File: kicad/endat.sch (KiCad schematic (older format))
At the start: 28 parts, among them J1901 tblock2x6, U1901 SI8662BD, U1904 SN75C1168DBR, U1905 SN75C1168DBR, U1908 SI8662BD

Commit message: touting....
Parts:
- added JP1902: jumper, Jumper:SolderJumper-3_P1.3mm_Open_RoundedPad1.0x1.5mm, symbol servo:Jumper_3_Bridged12
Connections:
- net labels added: ENDAT1_CLK_H_N, ENDAT1_CLK_H_P, ENDAT1_DATA_H_N, ENDAT1_DATA_H_P, ENDAT2_CLK_H_N, ENDAT2_CLK_H_P, ENDAT2_DATA_H_N, ENDAT2_DATA_H_P, Earth
- wire segments 180 -> 186
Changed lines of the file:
@@
 	1    0    0    -1
-$EndComp
-Wire Wire Line
-	7900 5450 7900 5400
-$Comp
-L servo:GNDH #PWR?
-U 1 1 5E51CFF4
-P 7900 5450
-AR Path="/5DE49152/5E51CFF4" Ref="#PWR?"  Part="1"
-AR Path="/5E1BAEAA/5E51CFF4" Ref="#PWR?"  Part="1"
-AR Path="/5DE3DF56/5E51CFF4" Ref="#PWR?"  Part="1"
-AR Path="/5F8D42C2/5E51CFF4" Ref="#PWR0222"  Part="1"
-F 0 "#PWR0222" H 7900 5200 30  0001 C CNN
-F 1 "GNDH" H 7900 5292 30  0000 C CNN
-F 2 "" H 7900 5450 50  0001 C CNN
-F 3 "" H 7900 5450 50  0001 C CNN
-	1    7900 5450
-	-1   0    0    -1
 $EndComp
 $Comp
@@
 	8050 4550 8150 4550
 Wire Wire Line
-	7800 5000 8100 5000
-Wire Wire Line
 	7900 5400 8100 5400
 $Comp
@@
 	1    0    0    -1
 $EndComp
-Wire Wire Line
-	7650 5100 8100 5100
-Wire Wire Line
-	7650 5200 7650 5250
-Wire Wire Line
-	7650 5200 8100 5200
-Wire Wire Line
-	7800 5300 8100 5300
-Wire Wire Line
-	8800 5450 8800 5400
-$Comp
-L servo:GNDH #PWR?
-U 1 1 5E607856
-P 8800 5450
-AR Path="/5DE49152/5E607856" Ref="#PWR?"  Part="1"
-AR Path="/5E1BAEAA/5E607856" Ref="#PWR?"  Part="1"
-AR Path="/5DE3DF56/5E607856" Ref="#PWR?"  Part="1"
-AR Path="/5F8D42C2/5E607856" Ref="#PWR0224"  Part="1"
-F 0 "#PWR0224" H 8800 5200 30  0001 C CNN
-F 1 "GNDH" H 8800 5292 30  0000 C CNN
-F 2 "" H 8800 5450 50  0001 C CNN
-F 3 "" H 8800 5450 50  0001 C CNN
-	1    8800 5450
-	1    0    0    -1
-$EndComp
-Wire Wire Line
-	8800 5400 8600 5400
 Text Label 4350 4550 0    39   ~ 0
 ENDAT1_MISO_H
@@
 	7100 4150 7300 4150
 Connection ~ 7300 4150
-Wire Wire Line
-	7650 5050 7650 5100
-Wire Wire Line
-	7800 4950 7800 5000
-Wire Wire Line
-	6850 5050 7200 5050
-Wire Wire Line
-	6750 4950 7100 4950
-Wire Wire Line
-	7100 4150 7100 4950
-Connection ~ 7100 4950
-Wire Wire Line
-	7100 4950 7800 4950
-Connection ~ 7200 5050
-Wire Wire Line
-	7200 5050 7650 5050
 $Comp
 L servo:R_Small R?
@@
 	7450 4150 7650 4150
 Connection ~ 7650 4150
-Wire Wire Line
-	7200 4350 7200 5050
-Wire Wire Line
-	7800 5350 7800 5300
-Wire Wire Line
-	6550 5250 7450 5250
-Wire Wire Line
-	6550 5350 7550 5350
-Wire Wire Line
-	7550 4350 7550 5350
-Connection ~ 7550 5350
-Wire Wire Line
-	7550 5350 7800 5350
-Wire Wire Line
-	7450 4150 7450 5250
-Connection ~ 7450 5250
-Wire Wire Line
-	7450 5250 7650 5250
 NoConn ~ 13850 4250
 NoConn ~ 13850 4650
@@
 NoConn ~ 11250 5250
 NoConn ~ 11250 5350
-Wire Wire Line
-	9050 5100 8600 5100
-Wire Wire Line
-	9050 5200 9050 5250
-Wire Wire Line
-	9050 5200 8600 5200
 $Comp
 L servo:R_Small R?
@@
 	9600 4150 9400 4150
 Connection ~ 9400 4150
-Wire Wire Line
-	9050 5050 9050 5100
-Wire Wire Line
-	9600 4150 9600 4950
-Connection ~ 9600 4950
-Wire Wire Line
-	9600 4950 8900 4950
-Connection ~ 9500 5050
-Wire Wire Line
-	9500 5050 9050 5050
 $Comp
 L servo:R_Small R?
@@
 	9250 4150 9050 4150
 Connection ~ 9050 4150
-Wire Wire Line
-	9500 4350 9500 5050
-Wire Wire Line
-	9150 4350 9150 5350
-Connection ~ 9150 5350
-Wire Wire Line
-	9150 5350 8900 5350
-Wire Wire Line
-	9250 4150 9250 5250
-Connection ~ 9250 5250
-Wire Wire Line
-	9250 5250 9050 5250
-Wire Wire Line
-	8900 4950 8900 5000
-Wire Wire Line
-	8900 5000 8600 5000
-Wire Wire Line
-	8600 5300 8900 5300
-Wire Wire Line
-	8900 5300 8900 5350
-Wire Wire Line
-	9500 5050 9900 5050
-Wire Wire Line
-	9600 4950 10000 4950
-Wire Wire Line
-	9250 5250 10200 5250
-Wire Wire Line
-	9150 5350 10200 5350
+$Comp
+L servo:GNDH #PWR?
+U 1 1 5E31EAC9
+P 8700 5800
+AR Path="/5DDE8C5E/5E31EAC9" Ref="#PWR?"  Part="1"
+AR Path="/5E092156/5E31EAC9" Ref="#PWR?"  Part="1"
+AR Path="/5F8D42C2/5E31EAC9" Ref="#PWR0268"  Part="1"
+F 0 "#PWR0268" H 8700 5550 30  0001 C CNN
+F 1 "GNDH" H 8700 5650 20  0000 C CNN
+F 2 "" H 8700 5800 50  0001 C CNN
+F 3 "" H 8700 5800 50  0001 C CNN
+	1    8700 5800
+	-1   0    0    -1
+$EndComp
+$Comp
+L servo:Jumper_3_Bridged12 JP?
+U 1 1 5E31EACF
+P 8350 5700
+AR Path="/5E1BAEAA/5E31EACF" Ref="JP?"  Part="1"
+AR Path="/5E21534F/5E31EACF" Ref="JP?"  Part="1"
+AR Path="/5DE3DF56/5E31EACF" Ref="JP?"  Part="1"
+AR Path="/5F8D42C2/5E31EACF" Ref="JP1902"  Part="1"
+F 0 "JP1902" H 8350 5869 39  0000 C CNN
+F 1 "jumper" H 8350 5794 39  0000 C CNN
+F 2 "Jumper:SolderJumper-3_P1.3mm_Open_RoundedPad1.0x1.5mm" H 8150 5500 50  0001 C CNN
+F 3 "~" H 8250 5600 50  0001 C CNN
+	1    8350 5700
+	1    0    0    1
+$EndComp
+Wire Wire Line
+	8550 5700 8700 5700
+Wire Wire Line
+	8700 5700 8700 5800
+$Comp
+L servo:Earth #PWR?
+U 1 1 5E31EAD8
+P 8000 5800
+AR Path="/5E21534F/5E31EAD8" Ref="#PWR?"  Part="1"
+AR Path="/5DE3DF56/5E31EAD8" Ref="#PWR?"  Part="1"
+AR Path="/5F8D42C2/5E31EAD8" Ref="#PWR0269"  Part="1"
+F 0 "#PWR0269" H 8000 5550 20  0001 C CNN
+F 1 "Earth" H 8000 5650 20  0000 C CNN
+F 2 "" H 8000 5800 50  0001 C CNN
+F 3 "~" H 8000 5800 50  0001 C CNN
+	1    8000 5800
+	1    0    0    -1
+$EndComp
+Wire Wire Line
+	8150 5700 8000 5700
+Wire Wire Line
+	8000 5700 8000 5850
+Wire Wire Line
+	7900 5600 8350 5600
+Wire Wire Line
+	7900 5400 7900 5600
+Wire Wire Line
+	8800 5400 8800 5600
+Connection ~ 8350 5600
+Wire Wire Line
+	8350 5600 8800 5600
+Text Label 6900 4950 0    39   ~ 0
+ENDAT1_DATA_H_P
+Text Label 6900 5050 0    39   ~ 0
+ENDAT1_DATA_H_N
+Text Label 6850 5350 0    39   ~ 0
+ENDAT1_CLK_H_P
+Text Label 6850 5250 0    39   ~ 0
+ENDAT1_CLK_H_N
+Wire Wire Line
+	6750 4950 7450 4950
+Wire Wire Line
+	7450 4150 7450 4950
+Wire Wire Line
+	7550 4350 7550 5050
+Wire Wire Line
+	6850 5050 7550 5050
+Connection ~ 7550 5050
+Wire Wire Line
+	7550 5050 7800 5050
+Wire Wire Line
+	6550 5250 7200 5250
+Wire Wire Line
+	6550 5350 7100 5350
+Wire Wire Line
+	7100 4150 7100 5350
+Wire Wire Line
+	7200 4350 7200 5250
+Wire Wire Line
+	7100 5350 7950 5350
+Wire Wire Line
+	7950 5350 7950 5000
+Wire Wire Line
+	7950 5000 8100 5000
+Connection ~ 7100 5350
+Wire Wire Line
+	7200 5250 8000 5250
+Wire Wire Line
+	8000 5250 8000 5100
+Wire Wire Line
+	8000 5100 8100 5100
+Connection ~ 7200 5250
+Wire Wire Line
+	7450 4950 7900 4950
+Wire Wire Line
+	7900 4950 7900 5200
+Wire Wire Line
+	7900 5200 8100 5200
+Connection ~ 7450 4950
+Wire Wire Line
+	7800 5050 7800 5300
+Wire Wire Line
+	7800 5300 8100 5300
+Wire Wire Line
+	8600 5000 8900 5000
+Wire Wire Line
+	8900 5000 8900 5350
+Wire Wire Line
+	8850 5250 8850 5100
+Wire Wire Line
+	8850 5100 8600 5100
+Wire Wire Line
+	9000 4950 9000 5200
+Wire Wire Line
+	9000 5200 8600 5200
+Wire Wire Line
+	8600 5300 9050 5300
+Wire Wire Line
+	9050 5300 9050 5050
+Wire Wire Line
+	8850 5250 9500 5250
+Wire Wire Line
+	9150 4350 9150 5050
+Wire Wire Line
+	9050 5050 9150 5050
+Connection ~ 9150 5050
+Wire Wire Line
+	9150 5050 9900 5050
+Wire Wire Line
+	9250 4150 9250 4950
+Wire Wire Line
+	9000 4950 9250 4950
+Connection ~ 9250 4950
+Wire Wire Line
+	9250 4950 10000 4950
+Wire Wire Line
+	9500 4350 9500 5250
+Connection ~ 9500 5250
+Wire Wire Line
+	9500 5250 10200 5250
+Wire Wire Line
+	9600 4150 9600 5350
+Wire Wire Line
+	8900 5350 9600 5350
+Connection ~ 9600 5350
+Wire Wire Line
+	9600 5350 10200 5350
+Text Label 9350 4950 0    39   ~ 0
+ENDAT2_DATA_H_P
+Text Label 9350 5050 0    39   ~ 0
+ENDAT2_DATA_H_N
+Text Label 9250 5250 0    39   ~ 0
+ENDAT2_CLK_H_N
+Text Label 9250 5350 0    39   ~ 0
+ENDAT2_CLK_H_P
+Wire Wire Line
+	8600 5400 8800 5400
 $EndSCHEMATC

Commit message: roouting and more routing.... I think 4 layers WONT be enought
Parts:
- removed JP1901: jumper, Jumper:SolderJumper-3_P1.3mm_Open_RoundedPad1.0x1.5mm, symbol servo:Jumper_3_Bridged12
- added JP1901: jumper, servo:SolderJumper-2_P1.3mm_Open_RoundedPad1.0x1.5mm, symbol servo:jumper
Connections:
- net labels added: ENDAT_5VH
- net labels removed: 15VH
- wire segments 186 -> 185
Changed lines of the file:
@@
 	1    0    0    -1
 $EndComp
-$Comp
-L servo:Jumper_3_Bridged12 JP?
-U 1 1 5E51CFFA
-P 8350 4550
-AR Path="/5E1BAEAA/5E51CFFA" Ref="JP?"  Part="1"
-AR Path="/5DE3DF56/5E51CFFA" Ref="JP?"  Part="1"
-AR Path="/5F8D42C2/5E51CFFA" Ref="JP1901"  Part="1"
-F 0 "JP1901" H 8350 4719 39  0000 C CNN
-F 1 "jumper" H 8350 4644 39  0000 C CNN
-F 2 "Jumper:SolderJumper-3_P1.3mm_Open_RoundedPad1.0x1.5mm" H 8150 4350 50  0001 C CNN
-F 3 "~" H 8250 4450 50  0001 C CNN
-	1    8350 4550
-	1    0    0    -1
-$EndComp
-$Comp
-L servo:15VH #PWR?
-U 1 1 5E51D001
-P 8650 4500
-AR Path="/5E1BAEAA/5E51D001" Ref="#PWR?"  Part="1"
-AR Path="/5DE3DF56/5E51D001" Ref="#PWR?"  Part="1"
-AR Path="/5F8D42C2/5E51D001" Ref="#PWR0223"  Part="1"
-F 0 "#PWR0223" H 8650 4300 20  0001 C CNN
-F 1 "15VH" H 8650 4657 28  0000 C CNN
-F 2 "" H 8650 4500 50  0001 C CNN
-F 3 "" H 8650 4500 50  0001 C CNN
-	1    8650 4500
-	1    0    0    -1
-$EndComp
-Wire Wire Line
-	8650 4550 8650 4500
-Wire Wire Line
-	8550 4550 8650 4550
 Wire Wire Line
 	8050 4500 8050 4550
@@
 	7950 4900 7950 4650
 Wire Wire Line
-	7950 4650 8350 4650
-Wire Wire Line
-	8350 4650 8750 4650
-Wire Wire Line
 	8750 4650 8750 4900
 Wire Wire Line
 	8750 4900 8600 4900
-Connection ~ 8350 4650
 Wire Wire Line
 	4300 4150 7000 4150
@@
 L servo:Earth #PWR?
 U 1 1 5E31EAD8
-P 8000 5800
+P 8050 5800
 AR Path="/5E21534F/5E31EAD8" Ref="#PWR?"  Part="1"
 AR Path="/5DE3DF56/5E31EAD8" Ref="#PWR?"  Part="1"
 AR Path="/5F8D42C2/5E31EAD8" Ref="#PWR0269"  Part="1"
-F 0 "#PWR0269" H 8000 5550 20  0001 C CNN
-F 1 "Earth" H 8000 5650 20  0000 C CNN
-F 2 "" H 8000 5800 50  0001 C CNN
-F 3 "~" H 8000 5800 50  0001 C CNN
-	1    8000 5800
-	1    0    0    -1
-$EndComp
-Wire Wire Line
-	8150 5700 8000 5700
-Wire Wire Line
-	8000 5700 8000 5850
+F 0 "#PWR0269" H 8050 5550 20  0001 C CNN
+F 1 "Earth" H 8050 5650 20  0000 C CNN
+F 2 "" H 8050 5800 50  0001 C CNN
+F 3 "~" H 8050 5800 50  0001 C CNN
+	1    8050 5800
+	1    0    0    -1
+$EndComp
 Wire Wire Line
 	7900 5600 8350 5600
@@
 Wire Wire Line
 	8600 5400 8800 5400
+$Comp
+L servo:jumper JP?
+U 1 1 5E2E6204
+P 8250 4550
+AR Path="/5DD76B18/5E2E6204" Ref="JP?"  Part="1"
+AR Path="/5F8D42C2/5E2E6204" Ref="JP1901"  Part="1"
+F 0 "JP1901" H 8250 4711 39  0000 C CNN
+F 1 "jumper" H 8250 4636 39  0000 C CNN
+F 2 "servo:SolderJumper-2_P1.3mm_Open_RoundedPad1.0x1.5mm" H 8150 4530 50  0001 C CNN
+F 3 "~" H 8250 4630 50  0001 C CNN
+	1    8250 4550
+	1    0    0    -1
+$EndComp
+Wire Wire Line
+	7950 4650 8350 4650
+Wire Wire Line
+	8350 4550 8350 4650
+Connection ~ 8350 4650
+Wire Wire Line
+	8350 4650 8750 4650
+Wire Wire Line
+	8050 5800 8050 5700
+Wire Wire Line
+	8050 5700 8150 5700
+Text Label 8450 4650 0    20   ~ 0
+ENDAT_5VH
 $EndSCHEMATC

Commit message: ROUTING DONE!!!!!!!!!!!!!!!!!!!!!!!!!
ok, but....I need to improve all the nets, get them wider and so, but at
least all nets were routed to the uController.. it was more difucult
than I ever imagine... it tooks me 1 week only the uC coarse layout..
very very complex.. a lot of traces.. and with NO blind vias.. so it'll
be cheaper and any prototype manufacturer could do the board, and it'll
be more reliable..AND I'd test all nets on the board it it has at least
one via, or rout alongside top or bottom, so it's all the nets.. for
debug, it's very important...
lets do some improvement...
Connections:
- net ENDAT1_MOSI_H: no longer U1901.15 (B1), U1904.15 (1D)
- new net: U1901.15 (B1), U1904.15 (1D)
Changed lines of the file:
@@
 Text Label 4350 4550 0    39   ~ 0
 ENDAT1_MISO_H
-Text Label 4350 4150 0    39   ~ 0
+Text Label 3200 4000 0    39   ~ 0
 ENDAT1_MOSI_H
 Text Label 4350 4450 0    39   ~ 0

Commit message: improvement...
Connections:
- net ENDAT1_MOSI_H: now also U1901.15 (B1), U1904.15 (1D)
- net ENDAT_GND: now reaches J1901.6a (Pin_6a), J1901.6b (Pin_6b), JP1902.2 (C)
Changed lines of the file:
@@
 Text Label 8450 4650 0    20   ~ 0
 ENDAT_5VH
+Text Label 8400 5600 0    20   ~ 0
+ENDAT_GND
+Text Label 4350 4150 0    39   ~ 0
+ENDAT1_MOSI_H
 $EndSCHEMATC

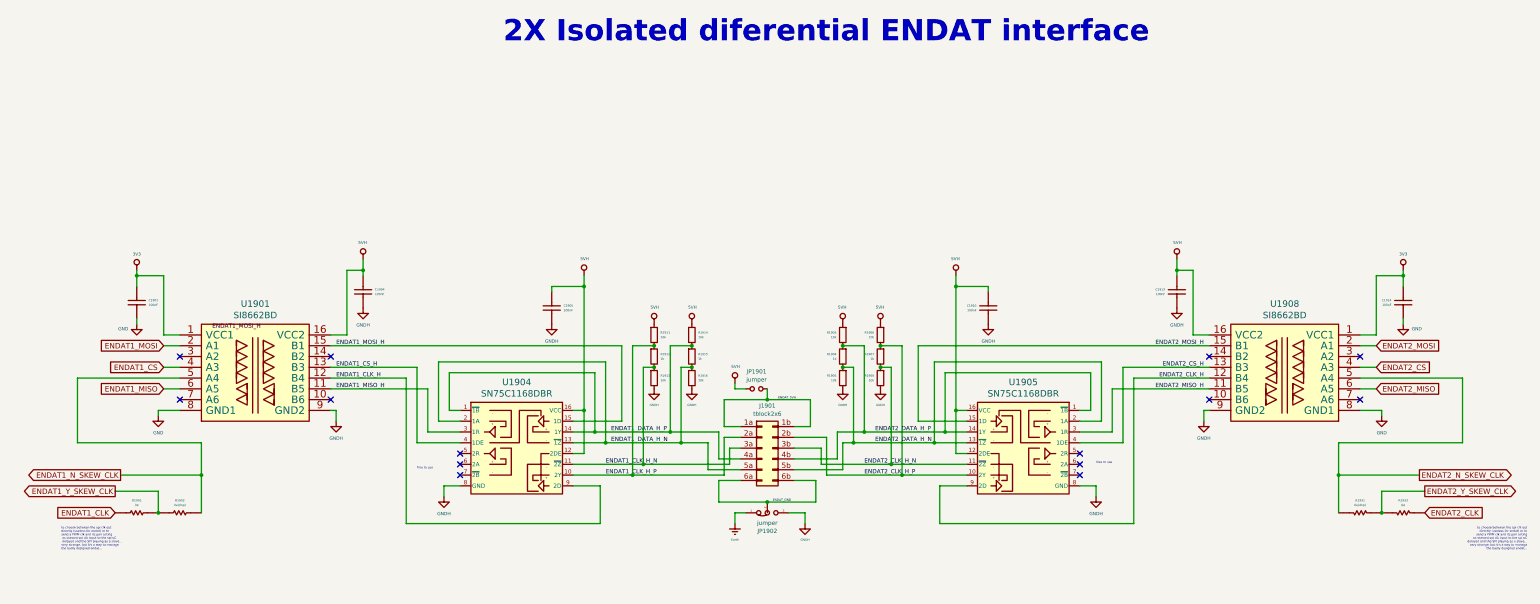
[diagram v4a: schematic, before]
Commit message: change in 5v interface scenario.. remove bridges
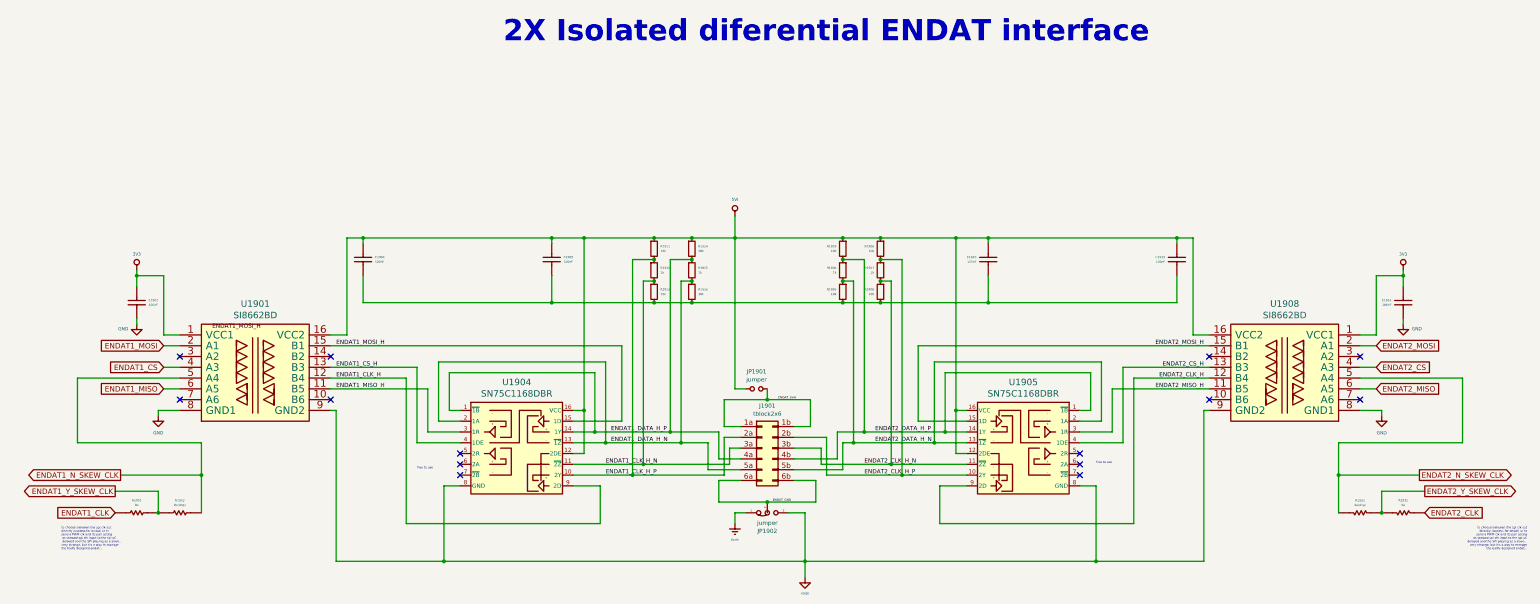
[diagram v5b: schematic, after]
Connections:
- net 5VH renamed 5VI
- net GNDH: no longer names the net of C1904.1, C1905.1, C1910.1, C1913.1, R1905.2, R1908.2, R1913.2, R1916.2
- net GNDH: no longer JP1902.3 (B), U1901.9 (GND2), U1904.8 (GND), U1905.8 (GND), U1908.9 (GND2)
- new net GNDI: JP1902.3 (B), U1901.9 (GND2), U1904.8 (GND), U1905.8 (GND), U1908.9 (GND2)
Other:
- moved on the sheet: C1904, C1905, C1910, C1913, R1903, R1904, R1905, R1906, R1907, R1908, R1911, R1912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
